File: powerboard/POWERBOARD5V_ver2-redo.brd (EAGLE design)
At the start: 83 x 42 mm, 55 parts, among them IC1 TPS5420, IC2 TPS5420

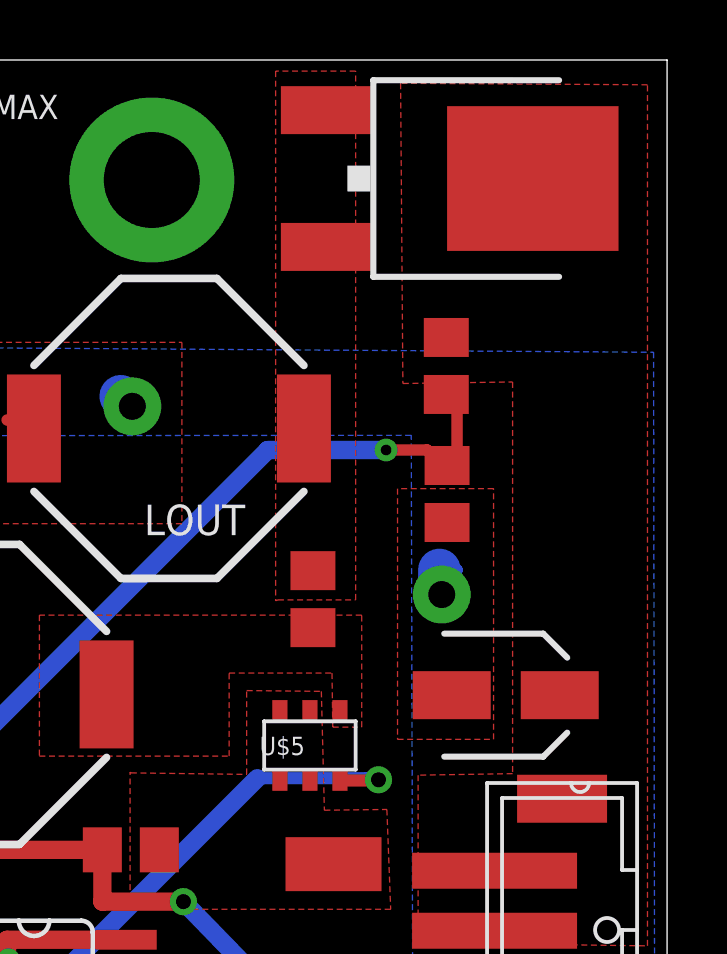
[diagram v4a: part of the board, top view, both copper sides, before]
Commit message: Added 2nd 56uF cap to powerboard, finished, needs DRC
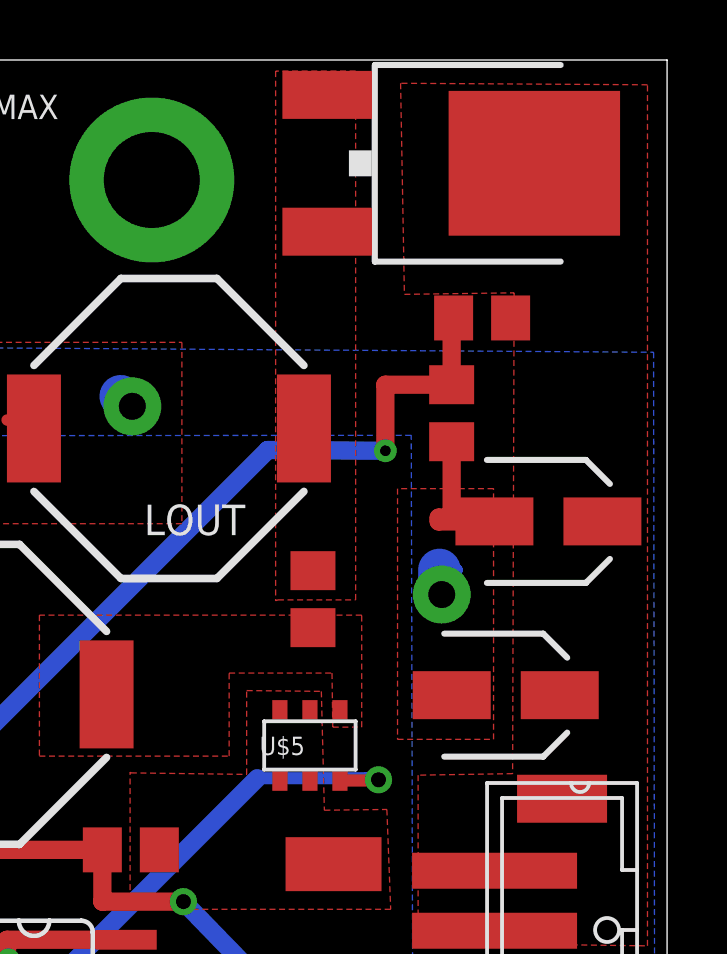
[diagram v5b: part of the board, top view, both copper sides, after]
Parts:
- added COUT1: 56uF, rcl:SANYO-OSCON_SMD_A5
- moved RFB1 2.70 mm to (75.8, 30.2)
- moved RFB2 2.00 mm to (76.8, 33.4), turned to 180 degrees
- moved U$6 0.51 mm to (77.0, 38.6)
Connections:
- net 6V: now also COUT1.+
- net GND: now also COUT1.-
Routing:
- net GND: track 28.4 -> 33.4 mm
- net FB: track 38.6 -> 40.0 mm
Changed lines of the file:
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@@
 <setting verticaltext="up"/>
 </settings>
-<grid distance="0.0254" unitdist="mm" unit="mm" style="lines" multiple="10" display="yes" altdistance="0.025" altunitdist="inch" altunit="inch"/>
+<grid distance="0.0254" unitdist="mm" unit="inch" style="lines" multiple="10" display="no" altdistance="0.025" altunitdist="inch" altunit="inch"/>
 <layers>
 <layer number="1" name="Top" color="4" fill="1" visible="yes" active="yes"/>
@@
 </element>
 <element name="COUT" library="rcl" package="SANYO-OSCON_SMD_A5" value="56uF" x="77.6224" y="20.828" smashed="yes">
-<attribute name="VALUE" x="78.6384" y="23.9522" size="0.6096" layer="27" rot="R180"/>
+<attribute name="VALUE" x="81.3054" y="23.5966" size="0.6096" layer="27" rot="R180"/>
 </element>
 <element name="LIN" library="SparkFun-Passives" package="SRU1038" value="6.2uH" x="59.817" y="20.8534"/>
@@
 <attribute name="VALUE" x="66.1162" y="17.5006" size="0.6096" layer="27" rot="R180"/>
 </element>
-<element name="RFB1" library="rcl" package="R0805" value="10k" x="75.6666" y="27.5336" smashed="yes" rot="R270">
-<attribute name="VALUE" x="77.0128" y="28.1178" size="0.6096" layer="27" rot="R270"/>
-</element>
-<element name="RFB2" library="rcl" package="R0805" value="37.4k" x="75.6412" y="31.8008" smashed="yes" rot="R270">
-<attribute name="VALUE" x="77.0636" y="32.4612" size="0.6096" layer="27" rot="R270"/>
-</element>
-<element name="U$6" library="ngohara_parts" package="DPAK" value="DPAK_DIODE" x="76.9366" y="38.0492" smashed="yes" rot="R270">
-<attribute name="VALUE" x="82.6262" y="37.1412" size="0.4064" layer="27" rot="R90"/>
+<element name="RFB1" library="rcl" package="R0805" value="10k" x="75.819" y="30.226" smashed="yes" rot="R270">
+<attribute name="VALUE" x="77.1652" y="30.8102" size="0.6096" layer="27" rot="R270"/>
+</element>
+<element name="RFB2" library="rcl" package="R0805" value="37.4k" x="76.835" y="33.401" smashed="yes" rot="R180">
+<attribute name="VALUE" x="79.1972" y="34.2646" size="0.6096" layer="27" rot="R270"/>
+</element>
+<element name="U$6" library="ngohara_parts" package="DPAK" value="DPAK_DIODE" x="76.9874" y="38.5572" smashed="yes" rot="R270">
+<attribute name="VALUE" x="82.677" y="37.6492" size="0.4064" layer="27" rot="R90"/>
 </element>
 <element name="CIN" library="rcl" package="C0805" value="22uF" x="40.8432" y="19.5326" smashed="yes" rot="R180">
@@
 <element name="U$4" library="jst-ph" package="JST-PH2-SMD" value="JST-PH2-SMD" x="82" y="10" rot="R90"/>
 <element name="U$7" library="jst-ph" package="JST-PH2-SMD" value="JST-PH2-SMD" x="82" y="0.9" rot="R90"/>
+<element name="COUT1" library="rcl" package="SANYO-OSCON_SMD_A5" value="56uF" x="79.0448" y="26.6192" smashed="yes"/>
 </elements>
 <signals>
@@
 <wire x1="75" y1="6" x2="77.25" y2="5.875" width="0.381" layer="1"/>
 <wire x1="76" y1="24" x2="75.4888" y2="24.1808" width="0.381" layer="16"/>
+<contactref element="COUT1" pad="-"/>
+<wire x1="75.819" y1="29.276" x2="75.819" y2="26.7462" width="0.6096" layer="1"/>
+<wire x1="75.819" y1="26.7462" x2="75.3872" y2="26.7462" width="0.6096" layer="1"/>
+<wire x1="75.3872" y1="26.7462" x2="75.3872" y2="26.6192" width="0.6096" layer="1"/>
+<wire x1="75.3872" y1="26.6192" x2="77.2448" y2="26.6192" width="0.6096" layer="1"/>
 </signal>
 <signal name="N$6">
@@
 <contactref element="RFB1" pad="1"/>
 <contactref element="RFB2" pad="2"/>
-<wire x1="76" y1="31" x2="76" y2="29" width="0.381" layer="1"/>
-<wire x1="76" y1="29" x2="75.6666" y2="28.4836" width="0.381" layer="1"/>
-<wire x1="76" y1="31" x2="75.6412" y2="30.8508" width="0.381" layer="1"/>
-<wire x1="75" y1="29" x2="73.635" y2="29" width="0.381" layer="1"/>
 <wire x1="58" y1="10" x2="58.8264" y2="10.1346" width="0.381" layer="1"/>
-<wire x1="75" y1="29" x2="75.6666" y2="28.4836" width="0.381" layer="1"/>
 <via x="56.2126" y="15.524" extent="1-16" drill="0.3556"/>
-<via x="73.635" y="29" extent="1-16" drill="0.3556"/>
+<via x="73.6096" y="28.9746" extent="1-16" drill="0.3556"/>
 <wire x1="58" y1="10" x2="55.118" y2="10" width="0.6096" layer="1"/>
 <wire x1="55.118" y1="10" x2="55.118" y2="15.4686" width="0.6096" layer="1"/>
@@
 <wire x1="56.2126" y1="15.4686" x2="56.2126" y2="15.524" width="0.6096" layer="1"/>
 <wire x1="56.2126" y1="15.524" x2="69.6886" y2="29" width="0.6096" layer="16"/>
-<wire x1="69.6886" y1="29" x2="73.635" y2="29" width="0.6096" layer="16"/>
+<wire x1="69.6886" y1="29" x2="73.6096" y2="28.9746" width="0.6096" layer="16"/>
+<wire x1="73.6096" y1="28.9746" x2="73.6096" y2="31.176" width="0.6096" layer="1"/>
+<wire x1="73.6096" y1="31.176" x2="75.819" y2="31.176" width="0.6096" layer="1"/>
+<wire x1="75.819" y1="31.176" x2="75.819" y2="33.401" width="0.6096" layer="1"/>
+<wire x1="75.819" y1="33.401" x2="75.885" y2="33.401" width="0.6096" layer="1"/>
 </signal>
 <signal name="LINSIG">
@@
 <vertex x="82.3468" y="41.1734"/>
 <vertex x="74.1172" y="41.2242"/>
-<vertex x="74.1934" y="31.2674"/>
-<vertex x="74.1934" y="31.2166"/>
-<vertex x="77.851" y="31.2674"/>
+<vertex x="74.2442" y="34.1884"/>
+<vertex x="77.9018" y="34.2392"/>
 <vertex x="77.851" y="18.2118"/>
 <vertex x="74.7014" y="18.161"/>
 <vertex x="74.7014" y="12.573"/>
 </polygon>
+<contactref element="COUT1" pad="+"/>
 </signal>
 <signal name="N$3">

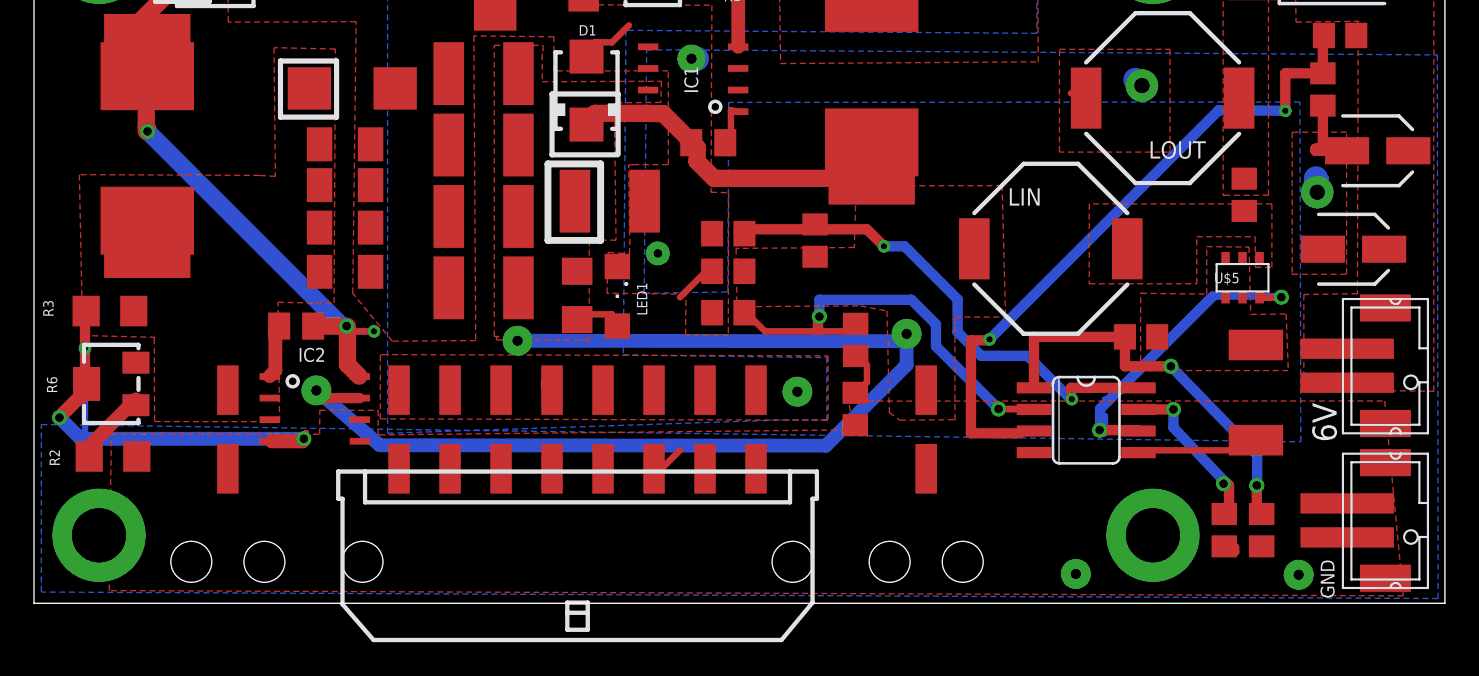
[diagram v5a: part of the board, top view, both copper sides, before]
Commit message: fixed fet, and fixed connector type
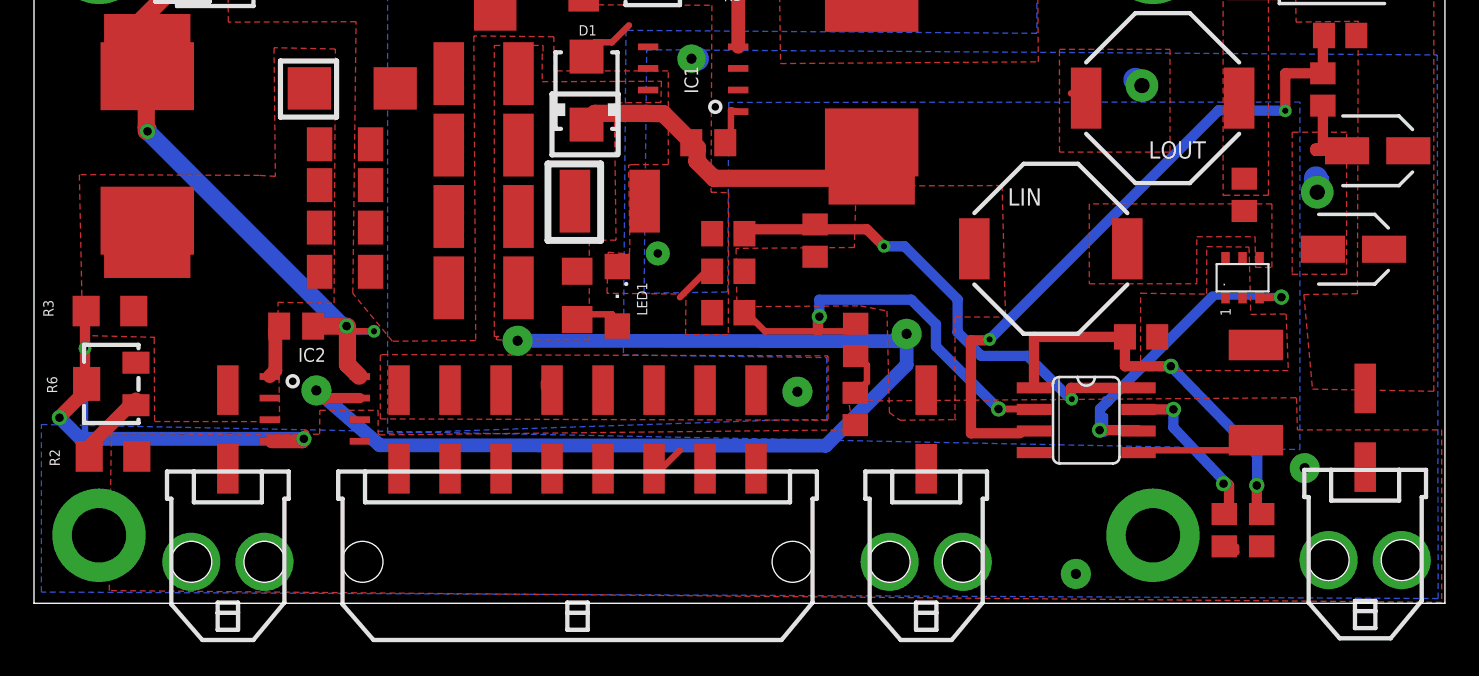
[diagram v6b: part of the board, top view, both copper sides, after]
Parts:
- removed U$4, U$7: JST-PH2-SMD, jst-ph:JST-PH2-SMD
- added X3: (no value), con-molex-micro-fit-3_0:43045-0206
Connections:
- net 6V: now also X3.P$2; no longer U$4.P$1, U$4.P$2
- net GND: now also X3.P$1; no longer U$7.P$1, U$7.P$2
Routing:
- net GND: track 33.4 -> 30.5 mm
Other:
- board text added: "."
- board text added: "1"
- board text removed: "6V"
- board text removed: "GND"
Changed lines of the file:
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@@
 <setting verticaltext="up"/>
 </settings>
-<grid distance="0.0254" unitdist="mm" unit="inch" style="lines" multiple="10" display="no" altdistance="0.025" altunitdist="inch" altunit="inch"/>
+<grid distance="0.1" unitdist="mm" unit="mm" style="lines" multiple="10" display="yes" altdistance="0.025" altunitdist="inch" altunit="inch"/>
 <layers>
 <layer number="1" name="Top" color="4" fill="1" visible="yes" active="yes"/>
@@
 <text x="24.1264" y="25.7052" size="1.016" layer="26" font="vector" ratio="16" rot="MR180">Wolfbot Swarm Robotics</text>
 <text x="26.3362" y="23.7494" size="1.016" layer="26" font="vector" ratio="16" rot="MR180">REV. June 23 2013</text>
-<text x="76.6318" y="9.4742" size="1.4224" layer="121" rot="R90">6V</text>
-<text x="76.5048" y="0.2794" size="0.8128" layer="121" rot="R90">GND</text>
+<text x="70.4" y="16.9" size="0.6096" layer="25" rot="R90">1</text>
+<text x="69.9" y="18.7" size="0.6096" layer="25">.</text>
 </plain>
 <attributes>
@@
 <element name="LIN" library="SparkFun-Passives" package="SRU1038" value="6.2uH" x="59.817" y="20.8534"/>
 <element name="LOUT" library="SparkFun-Passives" package="SRU1038" value="15uH" x="66.3956" y="29.718" rot="R180"/>
-<element name="U$5" library="ngohara_parts" package="TSOP-6" value="P-CHANNEL20V(D-S)MOSFET" x="71.0946" y="19.1516" smashed="yes">
-<attribute name="NAME" x="69.4186" y="18.8316" size="0.6096" layer="25"/>
-</element>
+<element name="U$5" library="ngohara_parts" package="TSOP-6" value="P-CHANNEL20V(D-S)MOSFET" x="71.0946" y="19.1516" smashed="yes"/>
 <element name="RBP" library="rcl" package="R0805" value="20.0" x="45.9486" y="21.336" smashed="yes" rot="R270">
 <attribute name="VALUE" x="47.371" y="22.479" size="0.6096" layer="27" rot="R270"/>
@@
 <attribute name="VALUE" x="69.469" y="11.8364" size="0.6096" layer="27" rot="R90"/>
 </element>
-<element name="U$4" library="jst-ph" package="JST-PH2-SMD" value="JST-PH2-SMD" x="82" y="10" rot="R90"/>
-<element name="U$7" library="jst-ph" package="JST-PH2-SMD" value="JST-PH2-SMD" x="82" y="0.9" rot="R90"/>
 <element name="COUT1" library="rcl" package="SANYO-OSCON_SMD_A5" value="56uF" x="79.0448" y="26.6192" smashed="yes"/>
+<element name="X3" library="con-molex-micro-fit-3_0" package="43045-0206" value="" x="78.3082" y="2.54"/>
 </elements>
 <signals>
@@
 </polygon>
 <polygon width="0.6096" layer="1">
-<vertex x="79.456" y="11.903"/>
-<vertex x="80.549" y="0.4366"/>
+<vertex x="82.8088" y="10.2012"/>
+<vertex x="82.8096" y="0.0556"/>
 <vertex x="4.4268" y="0.746"/>
 <vertex x="4.5508" y="9.9704"/>
@@
 <vertex x="48.2082" y="10.2036"/>
 <vertex x="47.9188" y="11.8938"/>
+<vertex x="74.2696" y="12.0904"/>
+<vertex x="74.3204" y="10.2012"/>
 </polygon>
 <contactref element="LED1" pad="C"/>
@@
 <contactref element="X1" pad="P$6"/>
 <contactref element="X1" pad="P$7"/>
-<contactref element="U$7" pad="P$2"/>
-<contactref element="U$7" pad="P$1"/>
 <polygon width="0.4064" layer="16">
 <vertex x="82.55" y="32.258"/>
@@
 <vertex x="0.4318" y="0.6604"/>
 <vertex x="0.4318" y="10.5156"/>
-<vertex x="74.5236" y="9.4996"/>
+<vertex x="74.4728" y="9.0424"/>
 <vertex x="74.4728" y="29.4894"/>
 <vertex x="40.8686" y="29.464"/>
@@
 </polygon>
 <via x="61.2902" y="1.7272" extent="1-16" drill="0.6" diameter="1.778"/>
-<via x="74.3966" y="1.6764" extent="1-16" drill="0.6" diameter="1.778"/>
+<via x="74.7522" y="7.9502" extent="1-16" drill="0.6" diameter="1.778"/>
 <wire x1="34" y1="33" x2="33" y2="33" width="0.381" layer="1"/>
 <wire x1="35" y1="34" x2="34" y2="33" width="0.381" layer="1"/>
@@
 <wire x1="40" y1="22" x2="39.8932" y2="21.7424" width="0.381" layer="1"/>
 <wire x1="40" y1="22" x2="39.77139375" y2="21.620578125" width="0.381" layer="1"/>
-<wire x1="77" y1="4" x2="77.25" y2="3.875" width="0.381" layer="1"/>
-<wire x1="77" y1="4" x2="77.2500125" y2="4" width="0.381" layer="1"/>
 <via x="36.6968" y="20.5814" extent="1-16" drill="0.5" diameter="1.4224"/>
 <via x="38.678" y="32.0368" extent="1-16" drill="0.6" diameter="1.6764"/>
@@
 <wire x1="70.7206" y1="3" x2="70.0206" y2="3.35" width="0.381" layer="1"/>
 <wire x1="70.7206" y1="3" x2="70.7206" y2="3.32979375" width="0.381" layer="1"/>
-<wire x1="75" y1="6" x2="75" y2="5.8750125" width="0.381" layer="1"/>
-<wire x1="75" y1="6" x2="77.25" y2="5.875" width="0.381" layer="1"/>
 <wire x1="76" y1="24" x2="75.4888" y2="24.1808" width="0.381" layer="16"/>
 <contactref element="COUT1" pad="-"/>
@@
 <wire x1="75.3872" y1="26.7462" x2="75.3872" y2="26.6192" width="0.6096" layer="1"/>
 <wire x1="75.3872" y1="26.6192" x2="77.2448" y2="26.6192" width="0.6096" layer="1"/>
+<contactref element="X3" pad="P$1"/>
 </signal>
 <signal name="N$6">
@@
 <contactref element="RFB2" pad="1"/>
 <contactref element="COUT" pad="+"/>
-<contactref element="U$4" pad="P$2"/>
-<contactref element="U$4" pad="P$1"/>
 <polygon width="0.4064" layer="1">
 <vertex x="82.3468" y="12.4714"/>
@@
 <vertex x="77.851" y="18.2118"/>
 <vertex x="74.7014" y="18.161"/>
-<vertex x="74.7014" y="12.573"/>
+<vertex x="75.2094" y="12.5984"/>
 </polygon>
 <contactref element="COUT1" pad="+"/>
+<contactref element="X3" pad="P$2"/>
 </signal>
 <signal name="N$3">

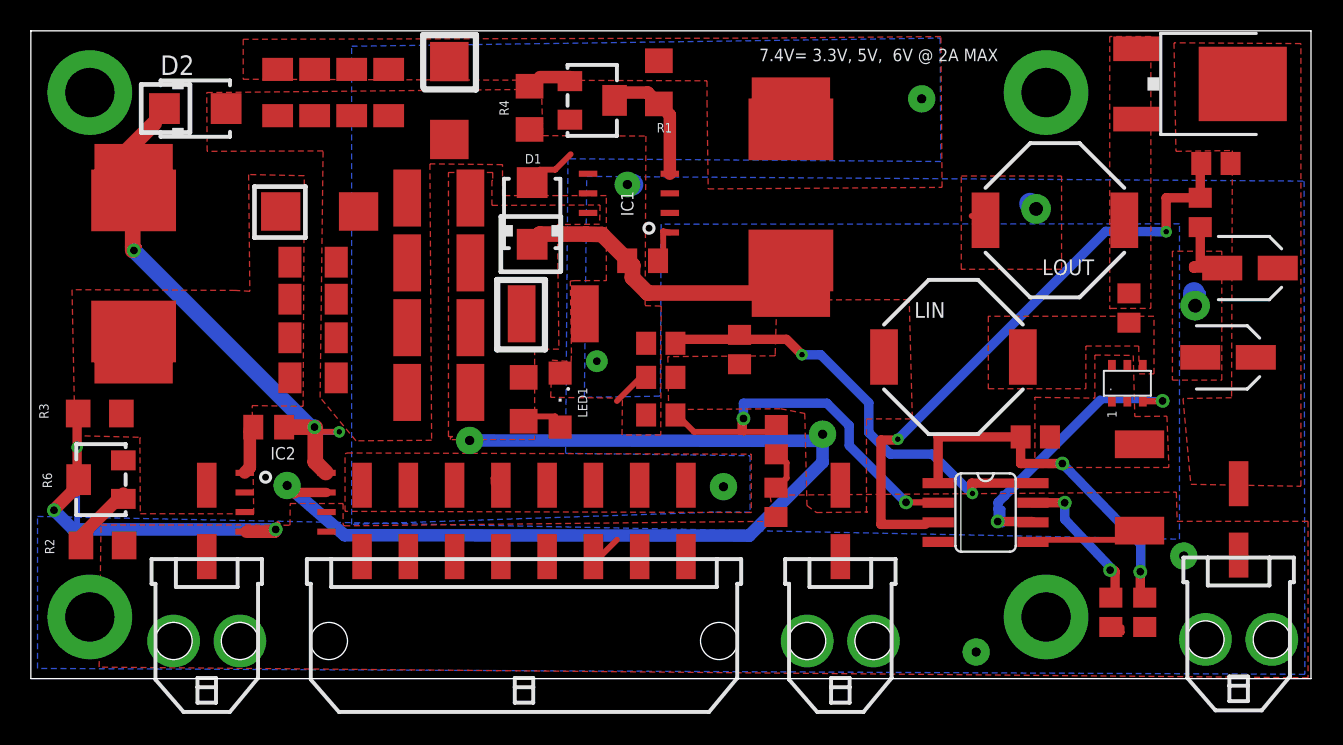
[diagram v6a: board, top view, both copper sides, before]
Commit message: resolved Sparkfun DRC errors, except for in-between pin errors
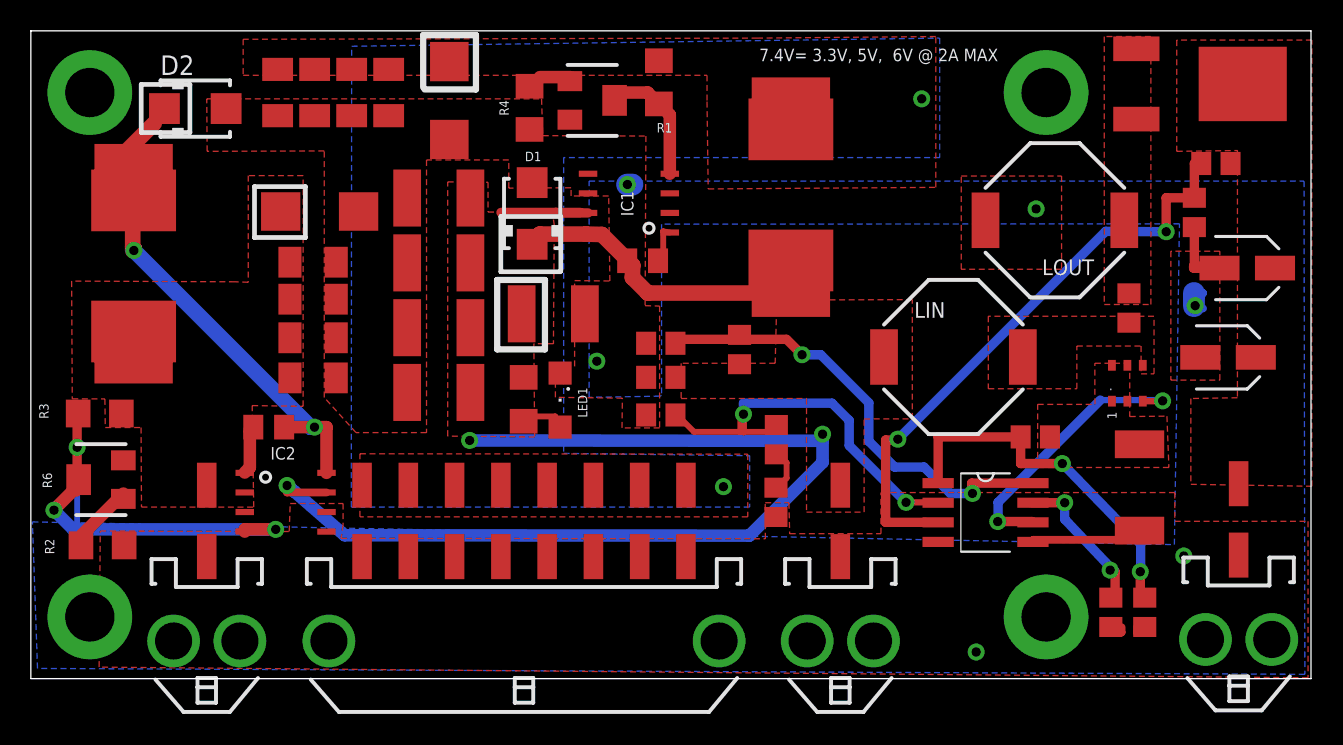
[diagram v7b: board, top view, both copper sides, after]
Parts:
- moved RFB1 0.38 mm to (75.4, 30.2)
- moved COUT1 0.18 mm to (78.9, 26.6)
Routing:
- net GND: track 30.5 -> 19.1 mm
- net V_BATT: track 66.1 -> 73.6 mm
- net N$13: track 38.8 -> 35.5 mm, vias 3 -> 2
- net N$23: track 20.6 -> 19.4 mm
- net 5V: track 1.01 -> 0.00 mm
- net 3_3V: track 0.96 -> 0.00 mm
- net FB: track 40.0 -> 39.3 mm
- net N$12: track 31.1 -> 30.5 mm
